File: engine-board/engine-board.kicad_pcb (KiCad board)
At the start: 2 copper layers, 217.2 x 60.3 mm, 31 parts, among them J10 USB/SER/CHRGR, J11 Engine Current Sensor, J12 Micro-Fit_2x04, J20 POWER_JACK, J21 73099-0, J22 73099-0, J24 Battery Input, J25 Turbine ESC, J27 Leak Detector, J28 Maxon Motor, J31 Solenoid, J32 Solenoid Current Sensor, J33 BME280 Sensor, J34 RV1805 Clock, J35 Reservoir Pressure Sensor, J36 Bladder Pressure Sensor, J37 VL6180 Range Sensor, J42 HMC6343 COMPASS, J43 NEO08MU GPS, J44 Turbine Current Sensor, Q1 IRLB8721PBF, U1 FEATHER_M0_BASIC_PROTO, U2 R-78B5.0-2.0, U3 R-78B3.3-2.0

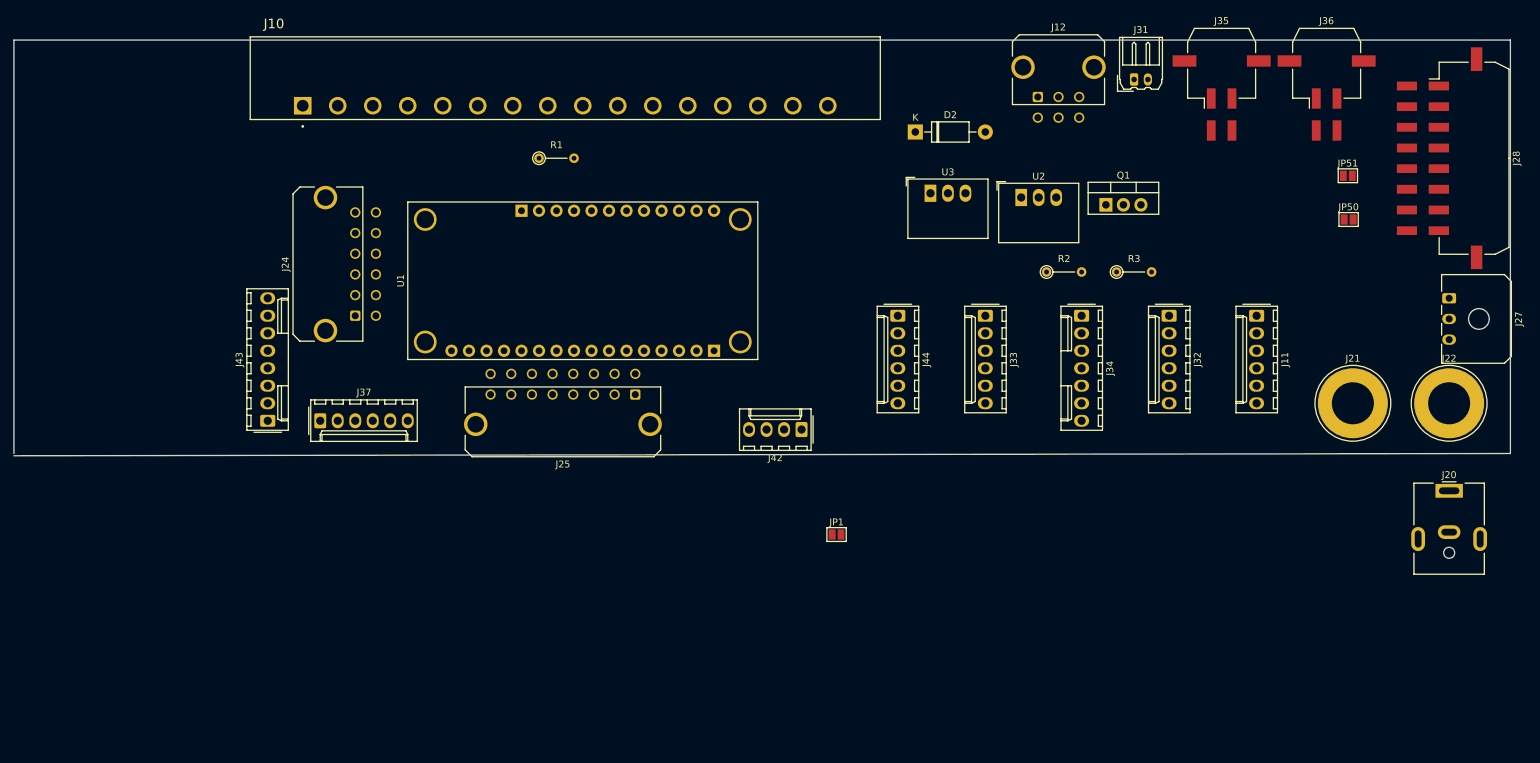
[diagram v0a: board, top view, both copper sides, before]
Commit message: all parts in schematic + pcb
still need to route + add mounting holes based on mechanical design.. ready for initial review
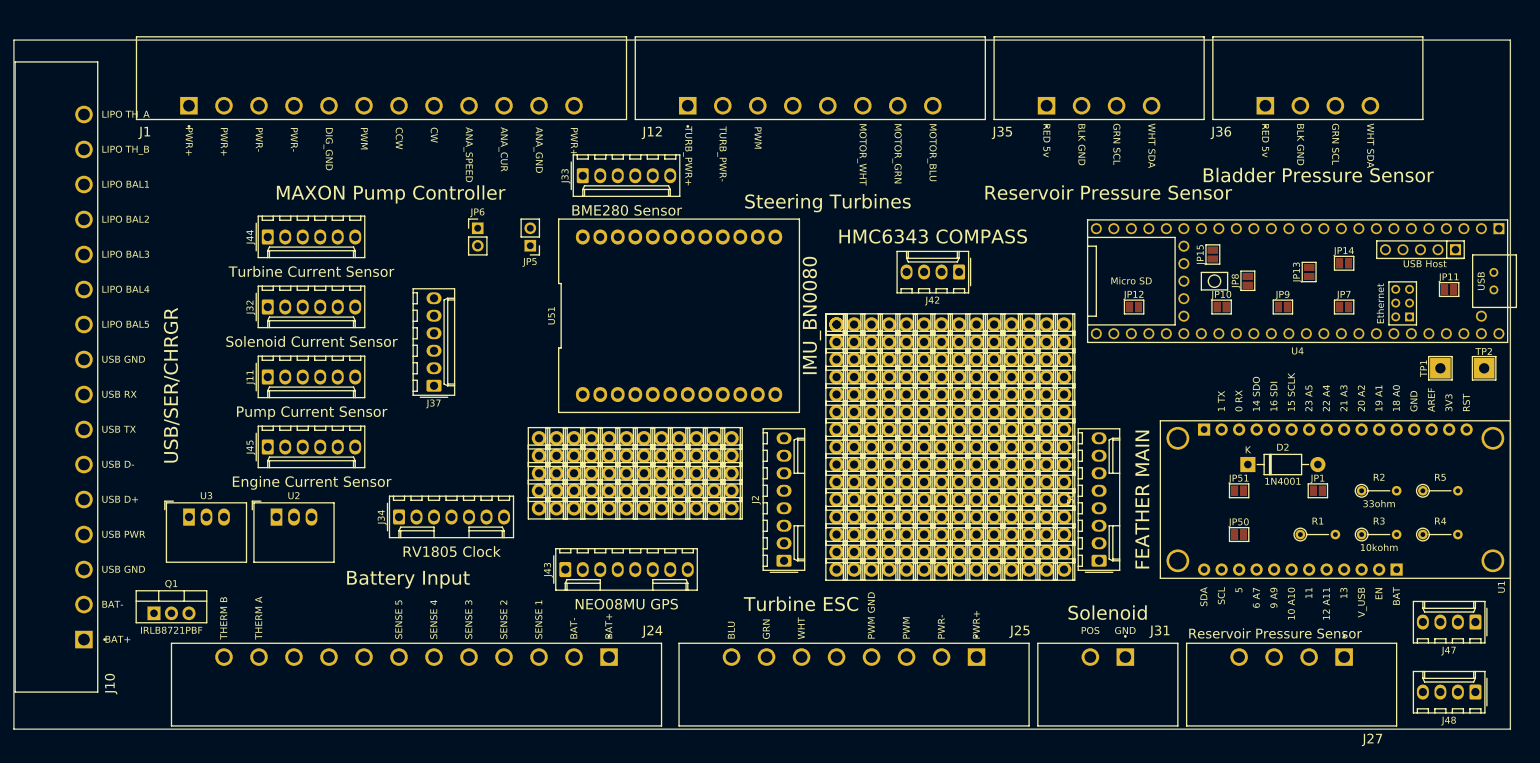
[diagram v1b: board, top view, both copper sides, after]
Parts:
- removed J20: POWER_JACK, Connector_BarrelJack:BarrelJack_CUI_PJ-063AH_Horizontal
- removed J21, J22: 73099-0, Connector:Banana_Jack_1Pin
- removed J28: Maxon Motor, Connector_Molex:Molex_Micro-Fit_3.0_43045-1610_2x08-1MP_P3.00mm_Horizontal
- added J1: MAXON Pump Controller, TerminalBlock_CUI:CUI_TBP01R1W-508-12BE, F.Cu at (58.4, 49.5)
- added J2: Power Rail, Connector_Molex:Molex_KK-254_AE-6410-08A_1x08_P2.54mm_Vertical, F.Cu at (144.8, 115.6)
- added J45: Engine Current Sensor, Connector_Molex:Molex_KK-254_AE-6410-06A_1x06_P2.54mm_Vertical, F.Cu at (69.8, 99.1)
- added J47: QWIIC 1, Connector_Molex:Molex_KK-254_AE-6410-04A_1x04_P2.54mm_Vertical, F.Cu at (245.1, 124.5)
- added J48: QWIIC 2, Connector_Molex:Molex_KK-254_AE-6410-04A_1x04_P2.54mm_Vertical, F.Cu at (245.1, 134.6)
- added J50: SD Card, Connector_Molex:Molex_KK-254_AE-6410-08A_1x08_P2.54mm_Vertical, F.Cu at (190.5, 115.6)
- added JP10: teensy_cw, Jumper:SolderJumper-2_P1.3mm_Open_Pad1.0x1.5mm, F.Cu at (208.3, 78.7)
- added JP11: pump_speed, Jumper:SolderJumper-2_P1.3mm_Open_Pad1.0x1.5mm, F.Cu at (241.3, 76.2)
- added JP12: pump_current, Jumper:SolderJumper-2_P1.3mm_Open_Pad1.0x1.5mm, F.Cu at (195.6, 78.7)
- added JP13: solenoid_gate, Jumper:SolderJumper-2_P1.3mm_Open_Pad1.0x1.5mm, F.Cu at (221.0, 73.7)
- added JP14: leak_in, Jumper:SolderJumper-2_P1.3mm_Open_Pad1.0x1.5mm, F.Cu at (226.1, 72.4)
- added JP15: imu_cs, Jumper:SolderJumper-2_P1.3mm_Open_Pad1.0x1.5mm, F.Cu at (207.0, 71.1)
- added JP5: IMU PS1 Jump, Connector_PinHeader_2.54mm:PinHeader_1x02_P2.54mm_Vertical, F.Cu at (108.0, 69.8)
- added JP6: IMU PS0 Jump, Connector_PinHeader_2.54mm:PinHeader_1x02_P2.54mm_Vertical, F.Cu at (100.3, 67.3)
- added JP7: teensy_scl, Jumper:SolderJumper-2_P1.3mm_Open_Pad1.0x1.5mm, F.Cu at (226.1, 78.7)
- added JP8: teensy sda, Jumper:SolderJumper-2_P1.3mm_Open_Pad1.0x1.5mm, F.Cu at (212.1, 74.9)
- added JP9: teensy_ccw, Jumper:SolderJumper-2_P1.3mm_Open_Pad1.0x1.5mm, F.Cu at (217.2, 78.7)
- added R4: 1kohm, Resistor_THT:R_Axial_DIN0204_L3.6mm_D1.6mm_P5.08mm_Vertical, F.Cu at (237.5, 111.8)
- added R5: 2kohm, Resistor_THT:R_Axial_DIN0204_L3.6mm_D1.6mm_P5.08mm_Vertical, F.Cu at (237.5, 105.4)
- added REF**: SIP-1, TestPoint:SIP-1, F.Cu at (137.2, 108.0)
- added REF**: SIP-1, TestPoint:SIP-1, F.Cu at (114.3, 108.0)
- added REF**: SIP-1, TestPoint:SIP-1, F.Cu at (160.0, 111.8)
- added REF**: SIP-1, TestPoint:SIP-1, F.Cu at (157.5, 111.8)
- added REF**: SIP-1, TestPoint:SIP-1, F.Cu at (154.9, 111.8)
- added REF**: SIP-1, TestPoint:SIP-1, F.Cu at (152.4, 111.8)
- added REF**: SIP-1, TestPoint:SIP-1, F.Cu at (185.4, 109.2)
- added REF**: SIP-1, TestPoint:SIP-1, F.Cu at (182.9, 109.2)
- added REF**: SIP-1, TestPoint:SIP-1, F.Cu at (180.3, 109.2)
- added REF**: SIP-1, TestPoint:SIP-1, F.Cu at (177.8, 109.2)
- added REF**: SIP-1, TestPoint:SIP-1, F.Cu at (175.3, 109.2)
- added REF**: SIP-1, TestPoint:SIP-1, F.Cu at (172.7, 109.2)
- added REF**: SIP-1, TestPoint:SIP-1, F.Cu at (111.8, 108.0)
- added REF**: SIP-1, TestPoint:SIP-1, F.Cu at (170.2, 109.2)
- added REF**: SIP-1, TestPoint:SIP-1, F.Cu at (167.6, 109.2)
- added REF**: SIP-1, TestPoint:SIP-1, F.Cu at (165.1, 109.2)
- added REF**: SIP-1, TestPoint:SIP-1, F.Cu at (162.6, 109.2)
- added REF**: SIP-1, TestPoint:SIP-1, F.Cu at (160.0, 109.2)
- added REF**: SIP-1, TestPoint:SIP-1, F.Cu at (157.5, 109.2)
- added REF**: SIP-1, TestPoint:SIP-1, F.Cu at (154.9, 109.2)
- added REF**: SIP-1, TestPoint:SIP-1, F.Cu at (152.4, 109.2)
- added REF**: SIP-1, TestPoint:SIP-1, F.Cu at (185.4, 106.7)
- added REF**: SIP-1, TestPoint:SIP-1, F.Cu at (182.9, 106.7)
- added REF**: SIP-1, TestPoint:SIP-1, F.Cu at (109.2, 108.0)
- added REF**: SIP-1, TestPoint:SIP-1, F.Cu at (180.3, 106.7)
- added REF**: SIP-1, TestPoint:SIP-1, F.Cu at (177.8, 106.7)
- added REF**: SIP-1, TestPoint:SIP-1, F.Cu at (175.3, 106.7)
- added REF**: SIP-1, TestPoint:SIP-1, F.Cu at (172.7, 106.7)
- added REF**: SIP-1, TestPoint:SIP-1, F.Cu at (170.2, 106.7)
- added REF**: SIP-1, TestPoint:SIP-1, F.Cu at (167.6, 106.7)
- added REF**: SIP-1, TestPoint:SIP-1, F.Cu at (165.1, 106.7)
- added REF**: SIP-1, TestPoint:SIP-1, F.Cu at (162.6, 106.7)
- added REF**: SIP-1, TestPoint:SIP-1, F.Cu at (160.0, 106.7)
- added REF**: SIP-1, TestPoint:SIP-1, F.Cu at (157.5, 106.7)
- added REF**: SIP-1, TestPoint:SIP-1, F.Cu at (137.2, 105.4)
- added REF**: SIP-1, TestPoint:SIP-1, F.Cu at (154.9, 106.7)
- added REF**: SIP-1, TestPoint:SIP-1, F.Cu at (152.4, 106.7)
- added REF**: SIP-1, TestPoint:SIP-1, F.Cu at (185.4, 104.1)
- added REF**: SIP-1, TestPoint:SIP-1, F.Cu at (182.9, 104.1)
- added REF**: SIP-1, TestPoint:SIP-1, F.Cu at (180.3, 104.1)
- added REF**: SIP-1, TestPoint:SIP-1, F.Cu at (177.8, 104.1)
- added REF**: SIP-1, TestPoint:SIP-1, F.Cu at (175.3, 104.1)
- added REF**: SIP-1, TestPoint:SIP-1, F.Cu at (172.7, 104.1)
- added REF**: SIP-1, TestPoint:SIP-1, F.Cu at (170.2, 104.1)
- added REF**: SIP-1, TestPoint:SIP-1, F.Cu at (167.6, 104.1)
- added REF**: SIP-1, TestPoint:SIP-1, F.Cu at (134.6, 105.4)
- added REF**: SIP-1, TestPoint:SIP-1, F.Cu at (165.1, 104.1)
- added REF**: SIP-1, TestPoint:SIP-1, F.Cu at (162.6, 104.1)
- added REF**: SIP-1, TestPoint:SIP-1, F.Cu at (160.0, 104.1)
- added REF**: SIP-1, TestPoint:SIP-1, F.Cu at (157.5, 104.1)
- added REF**: SIP-1, TestPoint:SIP-1, F.Cu at (154.9, 104.1)
- added REF**: SIP-1, TestPoint:SIP-1, F.Cu at (152.4, 104.1)
- added REF**: SIP-1, TestPoint:SIP-1, F.Cu at (185.4, 101.6)
- added REF**: SIP-1, TestPoint:SIP-1, F.Cu at (182.9, 101.6)
- added REF**: SIP-1, TestPoint:SIP-1, F.Cu at (180.3, 101.6)
- added REF**: SIP-1, TestPoint:SIP-1, F.Cu at (177.8, 101.6)
- added REF**: SIP-1, TestPoint:SIP-1, F.Cu at (132.1, 105.4)
- added REF**: SIP-1, TestPoint:SIP-1, F.Cu at (175.3, 101.6)
- added REF**: SIP-1, TestPoint:SIP-1, F.Cu at (172.7, 101.6)
- added REF**: SIP-1, TestPoint:SIP-1, F.Cu at (170.2, 101.6)
- added REF**: SIP-1, TestPoint:SIP-1, F.Cu at (167.6, 101.6)
- added REF**: SIP-1, TestPoint:SIP-1, F.Cu at (165.1, 101.6)
- added REF**: SIP-1, TestPoint:SIP-1, F.Cu at (162.6, 101.6)
- added REF**: SIP-1, TestPoint:SIP-1, F.Cu at (160.0, 101.6)
- added REF**: SIP-1, TestPoint:SIP-1, F.Cu at (157.5, 101.6)
- added REF**: SIP-1, TestPoint:SIP-1, F.Cu at (154.9, 101.6)
- added REF**: SIP-1, TestPoint:SIP-1, F.Cu at (152.4, 101.6)
- added REF**: SIP-1, TestPoint:SIP-1, F.Cu at (129.5, 105.4)
- added REF**: SIP-1, TestPoint:SIP-1, F.Cu at (185.4, 99.1)
- added REF**: SIP-1, TestPoint:SIP-1, F.Cu at (182.9, 99.1)
- added REF**: SIP-1, TestPoint:SIP-1, F.Cu at (180.3, 99.1)
- added REF**: SIP-1, TestPoint:SIP-1, F.Cu at (177.8, 99.1)
- added REF**: SIP-1, TestPoint:SIP-1, F.Cu at (175.3, 99.1)
- added REF**: SIP-1, TestPoint:SIP-1, F.Cu at (172.7, 99.1)
- added REF**: SIP-1, TestPoint:SIP-1, F.Cu at (170.2, 99.1)
- added REF**: SIP-1, TestPoint:SIP-1, F.Cu at (167.6, 99.1)
- added REF**: SIP-1, TestPoint:SIP-1, F.Cu at (165.1, 99.1)
- added REF**: SIP-1, TestPoint:SIP-1, F.Cu at (162.6, 99.1)
- added REF**: SIP-1, TestPoint:SIP-1, F.Cu at (127.0, 105.4)
- added REF**: SIP-1, TestPoint:SIP-1, F.Cu at (160.0, 99.1)
- added REF**: SIP-1, TestPoint:SIP-1, F.Cu at (157.5, 99.1)
- added REF**: SIP-1, TestPoint:SIP-1, F.Cu at (154.9, 99.1)
- added REF**: SIP-1, TestPoint:SIP-1, F.Cu at (152.4, 99.1)
- added REF**: SIP-1, TestPoint:SIP-1, F.Cu at (185.4, 96.5)
- added REF**: SIP-1, TestPoint:SIP-1, F.Cu at (182.9, 96.5)
- added REF**: SIP-1, TestPoint:SIP-1, F.Cu at (180.3, 96.5)
- added REF**: SIP-1, TestPoint:SIP-1, F.Cu at (177.8, 96.5)
- added REF**: SIP-1, TestPoint:SIP-1, F.Cu at (175.3, 96.5)
- added REF**: SIP-1, TestPoint:SIP-1, F.Cu at (172.7, 96.5)
- added REF**: SIP-1, TestPoint:SIP-1, F.Cu at (124.5, 105.4)
- added REF**: SIP-1, TestPoint:SIP-1, F.Cu at (170.2, 96.5)
- added REF**: SIP-1, TestPoint:SIP-1, F.Cu at (167.6, 96.5)
- added REF**: SIP-1, TestPoint:SIP-1, F.Cu at (165.1, 96.5)
- added REF**: SIP-1, TestPoint:SIP-1, F.Cu at (162.6, 96.5)
- added REF**: SIP-1, TestPoint:SIP-1, F.Cu at (160.0, 96.5)
- added REF**: SIP-1, TestPoint:SIP-1, F.Cu at (157.5, 96.5)
- added REF**: SIP-1, TestPoint:SIP-1, F.Cu at (154.9, 96.5)
- added REF**: SIP-1, TestPoint:SIP-1, F.Cu at (152.4, 96.5)
- added REF**: SIP-1, TestPoint:SIP-1, F.Cu at (185.4, 94.0)
- added REF**: SIP-1, TestPoint:SIP-1, F.Cu at (182.9, 94.0)
- added REF**: SIP-1, TestPoint:SIP-1, F.Cu at (121.9, 105.4)
- added REF**: SIP-1, TestPoint:SIP-1, F.Cu at (180.3, 94.0)
- added REF**: SIP-1, TestPoint:SIP-1, F.Cu at (177.8, 94.0)
- added REF**: SIP-1, TestPoint:SIP-1, F.Cu at (175.3, 94.0)
- added REF**: SIP-1, TestPoint:SIP-1, F.Cu at (172.7, 94.0)
- added REF**: SIP-1, TestPoint:SIP-1, F.Cu at (170.2, 94.0)
- added REF**: SIP-1, TestPoint:SIP-1, F.Cu at (167.6, 94.0)
- added REF**: SIP-1, TestPoint:SIP-1, F.Cu at (165.1, 94.0)
- added REF**: SIP-1, TestPoint:SIP-1, F.Cu at (162.6, 94.0)
- added REF**: SIP-1, TestPoint:SIP-1, F.Cu at (160.0, 94.0)
- added REF**: SIP-1, TestPoint:SIP-1, F.Cu at (157.5, 94.0)
- added REF**: SIP-1, TestPoint:SIP-1, F.Cu at (134.6, 108.0)
- added REF**: SIP-1, TestPoint:SIP-1, F.Cu at (119.4, 105.4)
- added REF**: SIP-1, TestPoint:SIP-1, F.Cu at (154.9, 94.0)
- added REF**: SIP-1, TestPoint:SIP-1, F.Cu at (152.4, 94.0)
- added REF**: SIP-1, TestPoint:SIP-1, F.Cu at (185.4, 91.4)
- added REF**: SIP-1, TestPoint:SIP-1, F.Cu at (182.9, 91.4)
- added REF**: SIP-1, TestPoint:SIP-1, F.Cu at (180.3, 91.4)
- added REF**: SIP-1, TestPoint:SIP-1, F.Cu at (177.8, 91.4)
- added REF**: SIP-1, TestPoint:SIP-1, F.Cu at (175.3, 91.4)
- added REF**: SIP-1, TestPoint:SIP-1, F.Cu at (172.7, 91.4)
- added REF**: SIP-1, TestPoint:SIP-1, F.Cu at (170.2, 91.4)
- added REF**: SIP-1, TestPoint:SIP-1, F.Cu at (167.6, 91.4)
- added REF**: SIP-1, TestPoint:SIP-1, F.Cu at (116.8, 105.4)
- added REF**: SIP-1, TestPoint:SIP-1, F.Cu at (165.1, 91.4)
- added REF**: SIP-1, TestPoint:SIP-1, F.Cu at (162.6, 91.4)
- added REF**: SIP-1, TestPoint:SIP-1, F.Cu at (160.0, 91.4)
- added REF**: SIP-1, TestPoint:SIP-1, F.Cu at (157.5, 91.4)
- added REF**: SIP-1, TestPoint:SIP-1, F.Cu at (154.9, 91.4)
- added REF**: SIP-1, TestPoint:SIP-1, F.Cu at (152.4, 91.4)
- added REF**: SIP-1, TestPoint:SIP-1, F.Cu at (185.4, 88.9)
- added REF**: SIP-1, TestPoint:SIP-1, F.Cu at (182.9, 88.9)
- added REF**: SIP-1, TestPoint:SIP-1, F.Cu at (180.3, 88.9)
- added REF**: SIP-1, TestPoint:SIP-1, F.Cu at (177.8, 88.9)
- added REF**: SIP-1, TestPoint:SIP-1, F.Cu at (114.3, 105.4)
- added REF**: SIP-1, TestPoint:SIP-1, F.Cu at (175.3, 88.9)
- added REF**: SIP-1, TestPoint:SIP-1, F.Cu at (172.7, 88.9)
- added REF**: SIP-1, TestPoint:SIP-1, F.Cu at (170.2, 88.9)
- added REF**: SIP-1, TestPoint:SIP-1, F.Cu at (167.6, 88.9)
- added REF**: SIP-1, TestPoint:SIP-1, F.Cu at (165.1, 88.9)
- added REF**: SIP-1, TestPoint:SIP-1, F.Cu at (162.6, 88.9)
- added REF**: SIP-1, TestPoint:SIP-1, F.Cu at (160.0, 88.9)
- added REF**: SIP-1, TestPoint:SIP-1, F.Cu at (157.5, 88.9)
- added REF**: SIP-1, TestPoint:SIP-1, F.Cu at (154.9, 88.9)
- added REF**: SIP-1, TestPoint:SIP-1, F.Cu at (152.4, 88.9)
- added REF**: SIP-1, TestPoint:SIP-1, F.Cu at (111.8, 105.4)
- added REF**: SIP-1, TestPoint:SIP-1, F.Cu at (185.4, 86.4)
- added REF**: SIP-1, TestPoint:SIP-1, F.Cu at (182.9, 86.4)
- added REF**: SIP-1, TestPoint:SIP-1, F.Cu at (180.3, 86.4)
- added REF**: SIP-1, TestPoint:SIP-1, F.Cu at (177.8, 86.4)
- added REF**: SIP-1, TestPoint:SIP-1, F.Cu at (175.3, 86.4)
- added REF**: SIP-1, TestPoint:SIP-1, F.Cu at (172.7, 86.4)
- added REF**: SIP-1, TestPoint:SIP-1, F.Cu at (170.2, 86.4)
- added REF**: SIP-1, TestPoint:SIP-1, F.Cu at (167.6, 86.4)
- added REF**: SIP-1, TestPoint:SIP-1, F.Cu at (165.1, 86.4)
- added REF**: SIP-1, TestPoint:SIP-1, F.Cu at (162.6, 86.4)
- added REF**: SIP-1, TestPoint:SIP-1, F.Cu at (109.2, 105.4)
- added REF**: SIP-1, TestPoint:SIP-1, F.Cu at (160.0, 86.4)
- added REF**: SIP-1, TestPoint:SIP-1, F.Cu at (157.5, 86.4)
- added REF**: SIP-1, TestPoint:SIP-1, F.Cu at (154.9, 86.4)
- added REF**: SIP-1, TestPoint:SIP-1, F.Cu at (152.4, 86.4)
- added REF**: SIP-1, TestPoint:SIP-1, F.Cu at (185.4, 83.8)
- added REF**: SIP-1, TestPoint:SIP-1, F.Cu at (182.9, 83.8)
- added REF**: SIP-1, TestPoint:SIP-1, F.Cu at (180.3, 83.8)
- added REF**: SIP-1, TestPoint:SIP-1, F.Cu at (177.8, 83.8)
- added REF**: SIP-1, TestPoint:SIP-1, F.Cu at (175.3, 83.8)
- added REF**: SIP-1, TestPoint:SIP-1, F.Cu at (172.7, 83.8)
- added REF**: SIP-1, TestPoint:SIP-1, F.Cu at (137.2, 102.9)
- added REF**: SIP-1, TestPoint:SIP-1, F.Cu at (170.2, 83.8)
- added REF**: SIP-1, TestPoint:SIP-1, F.Cu at (167.6, 83.8)
- added REF**: SIP-1, TestPoint:SIP-1, F.Cu at (165.1, 83.8)
- added REF**: SIP-1, TestPoint:SIP-1, F.Cu at (162.6, 83.8)
- added REF**: SIP-1, TestPoint:SIP-1, F.Cu at (160.0, 83.8)
- added REF**: SIP-1, TestPoint:SIP-1, F.Cu at (157.5, 83.8)
- added REF**: SIP-1, TestPoint:SIP-1, F.Cu at (154.9, 83.8)
- added REF**: SIP-1, TestPoint:SIP-1, F.Cu at (152.4, 83.8)
- added REF**: SIP-1, TestPoint:SIP-1, F.Cu at (185.4, 81.3)
- added REF**: SIP-1, TestPoint:SIP-1, F.Cu at (182.9, 81.3)
- added REF**: SIP-1, TestPoint:SIP-1, F.Cu at (134.6, 102.9)
- added REF**: SIP-1, TestPoint:SIP-1, F.Cu at (180.3, 81.3)
- added REF**: SIP-1, TestPoint:SIP-1, F.Cu at (177.8, 81.3)
- added REF**: SIP-1, TestPoint:SIP-1, F.Cu at (175.3, 81.3)
- added REF**: SIP-1, TestPoint:SIP-1, F.Cu at (172.7, 81.3)
- added REF**: SIP-1, TestPoint:SIP-1, F.Cu at (170.2, 81.3)
- added REF**: SIP-1, TestPoint:SIP-1, F.Cu at (167.6, 81.3)
- added REF**: SIP-1, TestPoint:SIP-1, F.Cu at (165.1, 81.3)
- added REF**: SIP-1, TestPoint:SIP-1, F.Cu at (162.6, 81.3)
- added REF**: SIP-1, TestPoint:SIP-1, F.Cu at (160.0, 81.3)
- added REF**: SIP-1, TestPoint:SIP-1, F.Cu at (157.5, 81.3)
- added REF**: SIP-1, TestPoint:SIP-1, F.Cu at (132.1, 102.9)
- added REF**: SIP-1, TestPoint:SIP-1, F.Cu at (154.9, 81.3)
- added REF** (x2): SIP-1, TestPoint:SIP-1, F.Cu at (152.4, 81.3)
- added REF**: SIP-1, TestPoint:SIP-1, F.Cu at (129.5, 102.9)
- added REF**: SIP-1, TestPoint:SIP-1, F.Cu at (127.0, 102.9)
- added REF**: SIP-1, TestPoint:SIP-1, F.Cu at (132.1, 108.0)
- added REF**: SIP-1, TestPoint:SIP-1, F.Cu at (124.5, 102.9)
- added REF**: SIP-1, TestPoint:SIP-1, F.Cu at (121.9, 102.9)
- added REF**: SIP-1, TestPoint:SIP-1, F.Cu at (119.4, 102.9)
- added REF**: SIP-1, TestPoint:SIP-1, F.Cu at (116.8, 102.9)
- added REF**: SIP-1, TestPoint:SIP-1, F.Cu at (114.3, 102.9)
- added REF**: SIP-1, TestPoint:SIP-1, F.Cu at (111.8, 102.9)
- added REF**: SIP-1, TestPoint:SIP-1, F.Cu at (109.2, 102.9)
- added REF**: SIP-1, TestPoint:SIP-1, F.Cu at (137.2, 100.3)
- added REF**: SIP-1, TestPoint:SIP-1, F.Cu at (134.6, 100.3)
- added REF**: SIP-1, TestPoint:SIP-1, F.Cu at (132.1, 100.3)
- added REF**: SIP-1, TestPoint:SIP-1, F.Cu at (129.5, 108.0)
- added REF**: SIP-1, TestPoint:SIP-1, F.Cu at (129.5, 100.3)
- added REF**: SIP-1, TestPoint:SIP-1, F.Cu at (127.0, 100.3)
- added REF**: SIP-1, TestPoint:SIP-1, F.Cu at (124.5, 100.3)
- added REF**: SIP-1, TestPoint:SIP-1, F.Cu at (121.9, 100.3)
- added REF**: SIP-1, TestPoint:SIP-1, F.Cu at (119.4, 100.3)
- added REF**: SIP-1, TestPoint:SIP-1, F.Cu at (116.8, 100.3)
- added REF**: SIP-1, TestPoint:SIP-1, F.Cu at (114.3, 100.3)
- added REF**: SIP-1, TestPoint:SIP-1, F.Cu at (111.8, 100.3)
- added REF**: SIP-1, TestPoint:SIP-1, F.Cu at (109.2, 100.3)
- added REF**: SIP-1, TestPoint:SIP-1, F.Cu at (137.2, 97.8)
- added REF**: SIP-1, TestPoint:SIP-1, F.Cu at (127.0, 108.0)
- added REF**: SIP-1, TestPoint:SIP-1, F.Cu at (134.6, 97.8)
- added REF**: SIP-1, TestPoint:SIP-1, F.Cu at (132.1, 97.8)
- added REF**: SIP-1, TestPoint:SIP-1, F.Cu at (129.5, 97.8)
- added REF**: SIP-1, TestPoint:SIP-1, F.Cu at (127.0, 97.8)
- added REF**: SIP-1, TestPoint:SIP-1, F.Cu at (124.5, 97.8)
- added REF**: SIP-1, TestPoint:SIP-1, F.Cu at (121.9, 97.8)
- added REF**: SIP-1, TestPoint:SIP-1, F.Cu at (119.4, 97.8)
- added REF**: SIP-1, TestPoint:SIP-1, F.Cu at (116.8, 97.8)
- added REF**: SIP-1, TestPoint:SIP-1, F.Cu at (114.3, 97.8)
- added REF**: SIP-1, TestPoint:SIP-1, F.Cu at (111.8, 97.8)
- added REF**: SIP-1, TestPoint:SIP-1, F.Cu at (124.5, 108.0)
- added REF**: SIP-1, TestPoint:SIP-1, F.Cu at (109.2, 97.8)
- added REF**: SIP-1, TestPoint:SIP-1, F.Cu at (185.4, 116.8)
- added REF**: SIP-1, TestPoint:SIP-1, F.Cu at (182.9, 116.8)
- added REF**: SIP-1, TestPoint:SIP-1, F.Cu at (180.3, 116.8)
- added REF**: SIP-1, TestPoint:SIP-1, F.Cu at (177.8, 116.8)
- added REF**: SIP-1, TestPoint:SIP-1, F.Cu at (175.3, 116.8)
- added REF**: SIP-1, TestPoint:SIP-1, F.Cu at (172.7, 116.8)
- added REF**: SIP-1, TestPoint:SIP-1, F.Cu at (170.2, 116.8)
- added REF**: SIP-1, TestPoint:SIP-1, F.Cu at (167.6, 116.8)
- added REF**: SIP-1, TestPoint:SIP-1, F.Cu at (121.9, 108.0)
- added REF**: SIP-1, TestPoint:SIP-1, F.Cu at (165.1, 116.8)
- added REF**: SIP-1, TestPoint:SIP-1, F.Cu at (162.6, 116.8)
- added REF**: SIP-1, TestPoint:SIP-1, F.Cu at (160.0, 116.8)
- added REF**: SIP-1, TestPoint:SIP-1, F.Cu at (157.5, 116.8)
- added REF**: SIP-1, TestPoint:SIP-1, F.Cu at (154.9, 116.8)
- added REF**: SIP-1, TestPoint:SIP-1, F.Cu at (152.4, 116.8)
- added REF**: SIP-1, TestPoint:SIP-1, F.Cu at (185.4, 114.3)
- added REF**: SIP-1, TestPoint:SIP-1, F.Cu at (182.9, 114.3)
- added REF**: SIP-1, TestPoint:SIP-1, F.Cu at (180.3, 114.3)
- added REF**: SIP-1, TestPoint:SIP-1, F.Cu at (177.8, 114.3)
- added REF**: SIP-1, TestPoint:SIP-1, F.Cu at (119.4, 108.0)
- added REF**: SIP-1, TestPoint:SIP-1, F.Cu at (175.3, 114.3)
- added REF**: SIP-1, TestPoint:SIP-1, F.Cu at (172.7, 114.3)
- added REF**: SIP-1, TestPoint:SIP-1, F.Cu at (170.2, 114.3)
- added REF**: SIP-1, TestPoint:SIP-1, F.Cu at (167.6, 114.3)
- added REF**: SIP-1, TestPoint:SIP-1, F.Cu at (165.1, 114.3)
- added REF**: SIP-1, TestPoint:SIP-1, F.Cu at (162.6, 114.3)
- added REF**: SIP-1, TestPoint:SIP-1, F.Cu at (160.0, 114.3)
- added REF**: SIP-1, TestPoint:SIP-1, F.Cu at (157.5, 114.3)
- added REF**: SIP-1, TestPoint:SIP-1, F.Cu at (154.9, 114.3)
- added REF**: SIP-1, TestPoint:SIP-1, F.Cu at (152.4, 114.3)
- added REF**: SIP-1, TestPoint:SIP-1, F.Cu at (116.8, 108.0)
- added REF**: SIP-1, TestPoint:SIP-1, F.Cu at (185.4, 111.8)
- added REF**: SIP-1, TestPoint:SIP-1, F.Cu at (182.9, 111.8)
- added REF**: SIP-1, TestPoint:SIP-1, F.Cu at (180.3, 111.8)
- added REF**: SIP-1, TestPoint:SIP-1, F.Cu at (177.8, 111.8)
- added REF**: SIP-1, TestPoint:SIP-1, F.Cu at (175.3, 111.8)
- added REF**: SIP-1, TestPoint:SIP-1, F.Cu at (172.7, 111.8)
- added REF**: SIP-1, TestPoint:SIP-1, F.Cu at (170.2, 111.8)
- added REF**: SIP-1, TestPoint:SIP-1, F.Cu at (167.6, 111.8)
- added REF**: SIP-1, TestPoint:SIP-1, F.Cu at (165.1, 111.8)
- added REF**: SIP-1, TestPoint:SIP-1, F.Cu at (162.6, 111.8)
- added TP1: raw leak, TestPoint:TestPoint_THTPad_3.0x3.0mm_Drill1.5mm, F.Cu at (240.0, 87.6)
- added TP2: leak3v3, TestPoint:TestPoint_THTPad_3.0x3.0mm_Drill1.5mm, F.Cu at (246.4, 87.6)
- added U4: Teensy4.1, Module:Teensy41, F.Cu at (219.3, 75.0)
- added U51: IMU_BN0080, Module:DIP-24_900_ELL, F.Cu at (129.5, 80.0)
- J11: value Engine Current Sensor -> Pump Current Sensor
- J12: value Micro-Fit_2x04 -> Steering Turbines; footprint Connector_Molex:Molex_Micro-Fit_3.0_43045-0621_2x03-1MP_P3.00mm_Horizontal -> TerminalBlock_CUI:CUI_TBP01R1W-508-08BE
- J24: footprint Connector_Molex:Molex_Micro-Fit_3.0_43045-1221_2x06-1MP_P3.00mm_Horizontal -> TerminalBlock_CUI:CUI_TBP01R1W-508-12BE
- J25: footprint Connector_Molex:Molex_Micro-Fit_3.0_43045-1621_2x08-1MP_P3.00mm_Horizontal -> TerminalBlock_CUI:CUI_TBP01R1W-508-08BE
- J27: value Leak Detector -> Reservoir Pressure Sensor; footprint Connector_Molex:Molex_Micro-Fit_3.0_43650-0300_1x03_P3.00mm_Horizontal -> TerminalBlock_CUI:CUI_TBP01R1W-508-04BE
- J31: footprint Connector_Molex:Molex_Micro-Latch_53254-0270_1x02_P2.00mm_Horizontal -> TerminalBlock_CUI:CUI_TBP01R1W-508-02BE
- J35, J36: footprint Connector_Molex:Molex_Micro-Fit_3.0_43045-0410_2x02-1MP_P3.00mm_Horizontal -> TerminalBlock_CUI:CUI_TBP01R1W-508-04BE
- JP50: value SolderJumper -> pump_pwm1
- JP51: value SolderJumper -> pump_pwm2
- moved Q1 150.3 mm to (53.3, 123.2)
- moved J11 143.8 mm to (69.8, 88.9), turned to 0 degrees
- moved J32 130.8 mm to (69.8, 78.7), turned to 0 degrees
- moved R1 123.2 mm to (219.7, 111.8)
- moved U2 117.6 mm to (71.1, 109.2)
- moved U3 117.4 mm to (58.4, 109.2)
- moved U1 113.7 mm to (224.8, 106.7), turned to 180 degrees
- moved J34 103.3 mm to (88.9, 109.2), turned to 0 degrees
- moved J44 92.2 mm to (69.8, 68.6), turned to 0 degrees
- moved J31 83.8 mm to (194.3, 129.5), turned to 180 degrees
- moved J10 83.7 mm to (43.2, 127.0), turned to 90 degrees
- moved JP1 70.1 mm to (222.2, 105.4)
- moved D2 68.2 mm to (212.1, 101.6)
- moved J25 62.5 mm to (172.7, 129.5)
- moved J33 61.9 mm to (115.6, 59.7), turned to 0 degrees
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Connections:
- net Net-(U1-Pad15) renamed /3v3_feather
- net Net-(U1-Pad24) renamed /pin7_feather
- net Net-(U1-Pad25) renamed /pin6_feather
- J11 pad 5: /engine_measured_BATT+ -> /pump_measured_BATT+
- J27 pad 2: +3V3 -> +5V
- U1 pad 1: -BATT -> Net-(U1-Pad1)
- U1 pad 26: Net-(U1-Pad26) -> /imu_cs
- U1 pad 28: (no net) -> /i2c_sda_1
- U1 pad 4: Net-(U1-Pad4) -> /SDO
- U1 pad 5: /leak_sense_output -> /SDI
- U1 pad 6: Net-(U1-Pad6) -> /SCK
- U1 pad 7: Net-(U1-Pad7) -> /sdcard_cs
- U1 pad 8: Net-(U1-Pad8) -> /leak_sense_output
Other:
- board size 217.2 x 60.3 mm -> 217.2 x 100 mm

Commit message: fixed size, mounting holes
size is 3"x12", mounting holes aligned with engine bracket, added IMU, Teensy, proper turbine PWM/speed control plugs, converted battery + turbine bulkhead connectors to Molex Minifit
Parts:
- removed the REF** at (137.2, 108.0)
- removed the REF** at (114.3, 108.0)
- removed the REF** at (160.0, 111.8)
- removed the REF** at (157.5, 111.8)
- removed the REF** at (154.9, 111.8)
- removed the REF** at (152.4, 111.8)
- removed the REF** at (185.4, 109.2)
- removed the REF** at (182.9, 109.2)
- removed the REF** at (180.3, 109.2)
- removed the REF** at (177.8, 109.2)
- removed the REF** at (175.3, 109.2)
- removed the REF** at (172.7, 109.2)
- removed the REF** at (111.8, 108.0)
- removed the REF** at (170.2, 109.2)
- removed the REF** at (167.6, 109.2)
- removed the REF** at (165.1, 109.2)
- removed the REF** at (162.6, 109.2)
- removed the REF** at (160.0, 109.2)
- removed the REF** at (157.5, 109.2)
- removed the REF** at (154.9, 109.2)
- removed the REF** at (152.4, 109.2)
- removed the REF** at (185.4, 106.7)
- removed the REF** at (182.9, 106.7)
- removed the REF** at (109.2, 108.0)
- removed the REF** at (180.3, 106.7)
- removed the REF** at (177.8, 106.7)
- removed the REF** at (175.3, 106.7)
- removed the REF** at (172.7, 106.7)
- removed the REF** at (170.2, 106.7)
- removed the REF** at (167.6, 106.7)
- removed the REF** at (165.1, 106.7)
- removed the REF** at (162.6, 106.7)
- removed the REF** at (160.0, 106.7)
- removed the REF** at (157.5, 106.7)
- removed the REF** at (137.2, 105.4)
- removed the REF** at (154.9, 106.7)
- removed the REF** at (152.4, 106.7)
- removed the REF** at (185.4, 104.1)
- removed the REF** at (182.9, 104.1)
- removed the REF** at (180.3, 104.1)
- removed the REF** at (177.8, 104.1)
- removed the REF** at (175.3, 104.1)
- removed the REF** at (172.7, 104.1)
- removed the REF** at (170.2, 104.1)
- removed the REF** at (167.6, 104.1)
- removed the REF** at (134.6, 105.4)
- removed the REF** at (165.1, 104.1)
- removed the REF** at (162.6, 104.1)
- removed the REF** at (160.0, 104.1)
- removed the REF** at (157.5, 104.1)
- removed the REF** at (154.9, 104.1)
- removed the REF** at (152.4, 104.1)
- removed the REF** at (185.4, 101.6)
- removed the REF** at (182.9, 101.6)
- removed the REF** at (180.3, 101.6)
- removed the REF** at (177.8, 101.6)
- removed the REF** at (132.1, 105.4)
- removed the REF** at (175.3, 101.6)
- removed the REF** at (172.7, 101.6)
- removed the REF** at (170.2, 101.6)
- removed the REF** at (167.6, 101.6)
- removed the REF** at (165.1, 101.6)
- removed the REF** at (162.6, 101.6)
- removed the REF** at (160.0, 101.6)
- removed the REF** at (157.5, 101.6)
- removed the REF** at (154.9, 101.6)
- removed the REF** at (152.4, 101.6)
- removed the REF** at (129.5, 105.4)
- removed the REF** at (185.4, 99.1)
- removed the REF** at (182.9, 99.1)
- removed the REF** at (180.3, 99.1)
- removed the REF** at (177.8, 99.1)
- removed the REF** at (175.3, 99.1)
- removed the REF** at (172.7, 99.1)
- removed the REF** at (170.2, 99.1)
- removed the REF** at (167.6, 99.1)
- removed the REF** at (165.1, 99.1)
- removed the REF** at (162.6, 99.1)
- removed the REF** at (127.0, 105.4)
- removed the REF** at (160.0, 99.1)
- removed the REF** at (157.5, 99.1)
- removed the REF** at (154.9, 99.1)
- removed the REF** at (152.4, 99.1)
- removed the REF** at (185.4, 96.5)
- removed the REF** at (182.9, 96.5)
- removed the REF** at (180.3, 96.5)
- removed the REF** at (177.8, 96.5)
- removed the REF** at (175.3, 96.5)
- removed the REF** at (172.7, 96.5)
- removed the REF** at (124.5, 105.4)
- removed the REF** at (170.2, 96.5)
- removed the REF** at (167.6, 96.5)
- removed the REF** at (165.1, 96.5)
- removed the REF** at (162.6, 96.5)
- removed the REF** at (160.0, 96.5)
- removed the REF** at (157.5, 96.5)
- removed the REF** at (154.9, 96.5)
- removed the REF** at (152.4, 96.5)
- removed the REF** at (185.4, 94.0)
- removed the REF** at (182.9, 94.0)
- removed the REF** at (121.9, 105.4)
- removed the REF** at (180.3, 94.0)
- removed the REF** at (177.8, 94.0)
- removed the REF** at (175.3, 94.0)
- removed the REF** at (172.7, 94.0)
- removed the REF** at (170.2, 94.0)
- removed the REF** at (167.6, 94.0)
- removed the REF** at (165.1, 94.0)
- removed the REF** at (162.6, 94.0)
- removed the REF** at (160.0, 94.0)
- removed the REF** at (157.5, 94.0)
- removed the REF** at (134.6, 108.0)
- removed the REF** at (119.4, 105.4)
- removed the REF** at (154.9, 94.0)
- removed the REF** at (152.4, 94.0)
- removed the REF** at (185.4, 91.4)
- removed the REF** at (182.9, 91.4)
- removed the REF** at (180.3, 91.4)
- removed the REF** at (177.8, 91.4)
- removed the REF** at (175.3, 91.4)
- removed the REF** at (172.7, 91.4)
- removed the REF** at (170.2, 91.4)
- removed the REF** at (167.6, 91.4)
- removed the REF** at (116.8, 105.4)
- removed the REF** at (165.1, 91.4)
- removed the REF** at (162.6, 91.4)
- removed the REF** at (160.0, 91.4)
- removed the REF** at (157.5, 91.4)
- removed the REF** at (154.9, 91.4)
- removed the REF** at (152.4, 91.4)
- removed the REF** at (185.4, 88.9)
- removed the REF** at (182.9, 88.9)
- removed the REF** at (180.3, 88.9)
- removed the REF** at (177.8, 88.9)
- removed the REF** at (114.3, 105.4)
- removed the REF** at (175.3, 88.9)
- removed the REF** at (172.7, 88.9)
- removed the REF** at (170.2, 88.9)
- removed the REF** at (167.6, 88.9)
- removed the REF** at (165.1, 88.9)
- removed the REF** at (162.6, 88.9)
- removed the REF** at (160.0, 88.9)
- removed the REF** at (157.5, 88.9)
- removed the REF** at (154.9, 88.9)
- removed the REF** at (152.4, 88.9)
- removed the REF** at (111.8, 105.4)
- removed the REF** at (185.4, 86.4)
- removed the REF** at (182.9, 86.4)
- removed the REF** at (180.3, 86.4)
- removed the REF** at (177.8, 86.4)
- removed the REF** at (175.3, 86.4)
- removed the REF** at (172.7, 86.4)
- removed the REF** at (170.2, 86.4)
- removed the REF** at (167.6, 86.4)
- removed the REF** at (165.1, 86.4)
- removed the REF** at (162.6, 86.4)
- removed the REF** at (109.2, 105.4)
- removed the REF** at (160.0, 86.4)
- removed the REF** at (157.5, 86.4)
- removed the REF** at (154.9, 86.4)
- removed the REF** at (152.4, 86.4)
- removed the REF** at (185.4, 83.8)
- removed the REF** at (182.9, 83.8)
- removed the REF** at (180.3, 83.8)
- removed the REF** at (177.8, 83.8)
- removed the REF** at (175.3, 83.8)
- removed the REF** at (172.7, 83.8)
- removed the REF** at (137.2, 102.9)
- removed the REF** at (170.2, 83.8)
- removed the REF** at (167.6, 83.8)
- removed the REF** at (165.1, 83.8)
- removed the REF** at (162.6, 83.8)
- removed the REF** at (160.0, 83.8)
- removed the REF** at (157.5, 83.8)
- removed the REF** at (154.9, 83.8)
- removed the REF** at (152.4, 83.8)
- removed the REF** at (185.4, 81.3)
- removed the REF** at (182.9, 81.3)
- removed the REF** at (134.6, 102.9)
- removed the REF** at (180.3, 81.3)
- removed the REF** at (177.8, 81.3)
- removed the REF** at (175.3, 81.3)
- removed the REF** at (172.7, 81.3)
- removed the REF** at (170.2, 81.3)
- removed the REF** at (167.6, 81.3)
- removed the REF** at (165.1, 81.3)
- removed the REF** at (162.6, 81.3)
- removed the REF** at (160.0, 81.3)
- removed the REF** at (157.5, 81.3)
- removed the REF** at (132.1, 102.9)
- removed the REF** at (154.9, 81.3)
- removed the REF** at (152.4, 81.3) (x2)
- removed the REF** at (129.5, 102.9)
- removed the REF** at (127.0, 102.9)
- removed the REF** at (132.1, 108.0)
- removed the REF** at (124.5, 102.9)
- removed the REF** at (121.9, 102.9)
- removed the REF** at (119.4, 102.9)
- removed the REF** at (116.8, 102.9)
- removed the REF** at (114.3, 102.9)
- removed the REF** at (111.8, 102.9)
- removed the REF** at (109.2, 102.9)
- removed the REF** at (137.2, 100.3)
- removed the REF** at (134.6, 100.3)
- removed the REF** at (132.1, 100.3)
- removed the REF** at (129.5, 108.0)
- removed the REF** at (129.5, 100.3)
- removed the REF** at (127.0, 100.3)
- removed the REF** at (124.5, 100.3)
- removed the REF** at (121.9, 100.3)
- removed the REF** at (119.4, 100.3)
- removed the REF** at (116.8, 100.3)
- removed the REF** at (114.3, 100.3)
- removed the REF** at (111.8, 100.3)
- removed the REF** at (109.2, 100.3)
- removed the REF** at (137.2, 97.8)
- removed the REF** at (127.0, 108.0)
- removed the REF** at (134.6, 97.8)
- removed the REF** at (132.1, 97.8)
- removed the REF** at (129.5, 97.8)
- removed the REF** at (127.0, 97.8)
- removed the REF** at (124.5, 97.8)
- removed the REF** at (121.9, 97.8)
- removed the REF** at (119.4, 97.8)
- removed the REF** at (116.8, 97.8)
- removed the REF** at (114.3, 97.8)
- removed the REF** at (111.8, 97.8)
- removed the REF** at (124.5, 108.0)
- removed the REF** at (109.2, 97.8)
- removed the REF** at (185.4, 116.8)
- removed the REF** at (182.9, 116.8)
- removed the REF** at (180.3, 116.8)
- removed the REF** at (177.8, 116.8)
- removed the REF** at (175.3, 116.8)
- removed the REF** at (172.7, 116.8)
- removed the REF** at (170.2, 116.8)
- removed the REF** at (167.6, 116.8)
- removed the REF** at (121.9, 108.0)
- removed the REF** at (165.1, 116.8)
- removed the REF** at (162.6, 116.8)
- removed the REF** at (160.0, 116.8)
- removed the REF** at (157.5, 116.8)
- removed the REF** at (154.9, 116.8)
- removed the REF** at (152.4, 116.8)
- removed the REF** at (185.4, 114.3)
- removed the REF** at (182.9, 114.3)
- removed the REF** at (180.3, 114.3)
- removed the REF** at (177.8, 114.3)
- removed the REF** at (119.4, 108.0)
- removed the REF** at (175.3, 114.3)
- removed the REF** at (172.7, 114.3)
- removed the REF** at (170.2, 114.3)
- removed the REF** at (167.6, 114.3)
- removed the REF** at (165.1, 114.3)
- removed the REF** at (162.6, 114.3)
- removed the REF** at (160.0, 114.3)
- removed the REF** at (157.5, 114.3)
- removed the REF** at (154.9, 114.3)
- removed the REF** at (152.4, 114.3)
- removed the REF** at (116.8, 108.0)
- removed the REF** at (185.4, 111.8)
- removed the REF** at (182.9, 111.8)
- removed the REF** at (180.3, 111.8)
- removed the REF** at (177.8, 111.8)
- removed the REF** at (175.3, 111.8)
- removed the REF** at (172.7, 111.8)
- removed the REF** at (170.2, 111.8)
- removed the REF** at (167.6, 111.8)
- removed the REF** at (165.1, 111.8)
- removed the REF** at (162.6, 111.8)
- added H1: MountingHole_5.3mm_M5, MountingHole:MountingHole_5.3mm_M5, F.Cu at (74.6, 149.2)
- added J53: Switch Bulkhead, TerminalBlock_CUI:CUI_TBP01R1W-508-02BE, F.Cu at (64.8, 154.9)
- added J62: Turbine 2 ESC, TerminalBlock_CUI:CUI_TBP01R1W-508-08BE, F.Cu at (121.9, 99.1)
- added REF**: MountingHole_5.3mm_M5, MountingHole:MountingHole_5.3mm_M5, F.Cu at (350.2, 104.8)
- added REF**: MountingHole_5.3mm_M5, MountingHole:MountingHole_5.3mm_M5, F.Cu at (349.9, 149.2)
- added REF**: MountingHole_5.3mm_M5, MountingHole:MountingHole_5.3mm_M5, F.Cu at (174.6, 149.2)
- added REF**: MountingHole_5.3mm_M5, MountingHole:MountingHole_5.3mm_M5, F.Cu at (274.9, 149.2)
- added REF**: MountingHole_5.3mm_M5, MountingHole:MountingHole_5.3mm_M5, F.Cu at (274.9, 104.8)
- added REF**: MountingHole_5.3mm_M5, MountingHole:MountingHole_5.3mm_M5, F.Cu at (174.6, 104.8)
- added REF**: MountingHole_5.3mm_M5, MountingHole:MountingHole_5.3mm_M5, F.Cu at (74.6, 104.8)
- added U10: Pololu_2812, Module:Pololu_SlidePwrSwitch, F.Cu at (227.3, 128.3)
- J10: footprint Connector_PinHeader_2.54mm:CUI_TBP01R1W-508-16BE -> Connector_Molex:Molex_Micro-Fit_3.0_43045-1600_2x08_P3.00mm_Horizontal
- J12: footprint TerminalBlock_CUI:CUI_TBP01R1W-508-08BE -> Connector_Molex:Molex_Micro-Fit_3.0_43045-0821_2x04-1MP_P3.00mm_Horizontal
- J27: value Reservoir Pressure Sensor -> Leak Sensor
- J61: renamed from J25; value Turbine ESC -> Turbine 1 ESC
- moved J1 231.2 mm to (284.5, 97.8)
- moved J43 172.5 mm to (284.5, 135.9), turned to 90 degrees
- moved JP5 149.2 mm to (236.2, 146.1)
- moved JP6 149.2 mm to (228.6, 143.5)
- moved Q1 138.5 mm to (189.2, 96.5)
- moved U51 138.2 mm to (259.1, 128.3)
- moved JP1 122.6 mm to (336.6, 149.9)
- moved JP15 118.4 mm to (316.2, 116.8), turned to 180 degrees
- moved JP10 118.4 mm to (317.5, 124.5)
- moved JP11 118.4 mm to (350.5, 121.9)
- moved JP12 118.4 mm to (304.8, 124.5)
- moved JP13 118.4 mm to (330.2, 119.4)
- moved JP14 118.4 mm to (335.3, 118.1)
- moved JP7 118.4 mm to (335.3, 124.5)
- moved JP8 118.4 mm to (321.3, 120.7)
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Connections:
- J12 pad 4: Net-(J12-Pad4) -> /external_switch_B
- J12 pad 8: Net-(J12-Pad8) -> /external_switch_A
- J24 pad 1: +BATT -> Net-(J24-Pad1)
- J24 pad 2: +BATT -> Net-(J24-Pad1)
- J24 pad 3: -BATT -> Net-(J24-Pad3)
- J24 pad 4: -BATT -> Net-(J24-Pad3)
- J61 pad 2: /turbine1_measured_pwr -> -BATT
- J61 pad 3: -BATT -> /turbine_1_pwm
- J61 pad 7: /turbine2_grn -> /turbine1_grn
- U1 pad 24: /pin7_feather -> /turbine_1_pwm
- U1 pad 25: /pin6_feather -> /turbine_2_pwm
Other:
- board size 217.2 x 100 mm -> 304.1 x 95.2 mm

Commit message: pushed everything to silkscreen from f.fab
almost final..  just needs routing..
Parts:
- removed REF** (x2): MountingHole_5.3mm_M5, MountingHole:MountingHole_5.3mm_M5
- added REF7: MountingHole_5.3mm_M5, MountingHole:MountingHole_5.3mm_M5, F.Cu at (350.2, 104.8)
- added REF8: MountingHole_5.3mm_M5, MountingHole:MountingHole_5.3mm_M5, F.Cu at (349.9, 149.2)
- JP1: value SolderJumper -> PumpAngGND
- moved J47 179.4 mm to (87.6, 160.0), turned to 0 degrees
- moved J48 179.4 mm to (87.6, 149.9), turned to 0 degrees
- moved JP5 29.2 mm to (265.4, 147.3)
- moved JP6 29.2 mm to (257.8, 144.8)
- moved U2 18.9 mm to (132.1, 121.9)
- moved U3 18.9 mm to (119.4, 121.9)
- moved J27 17.8 mm to (262.9, 156.2)
- moved J35 17.8 mm to (231.1, 156.2)
- moved J36 17.8 mm to (199.4, 156.2)
- moved J24 11.5 mm to (161.3, 156.2)
- moved R2 6.48 mm to (302.3, 133.3)
- moved JP50 5.08 mm to (317.5, 146.1)
- moved JP51 4.02 mm to (317.5, 152.4)
- moved D2 3.81 mm to (323.9, 144.8)
- moved R1 2.84 mm to (325.1, 153.7)
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- renumbered REF** to REF1, H1 to REF2, REF** to REF3, REF** to REF4, REF** to REF5, REF** to REF6
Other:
- board size 304.1 x 95.2 mm -> 304.1 x 76.2 mm
- net class power added: clearance 0.2, trace_width 1, via_dia 1, via_drill 0.4
